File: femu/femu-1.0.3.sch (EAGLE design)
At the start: 54 parts, among them IC1 ESP32-QFN_5X5

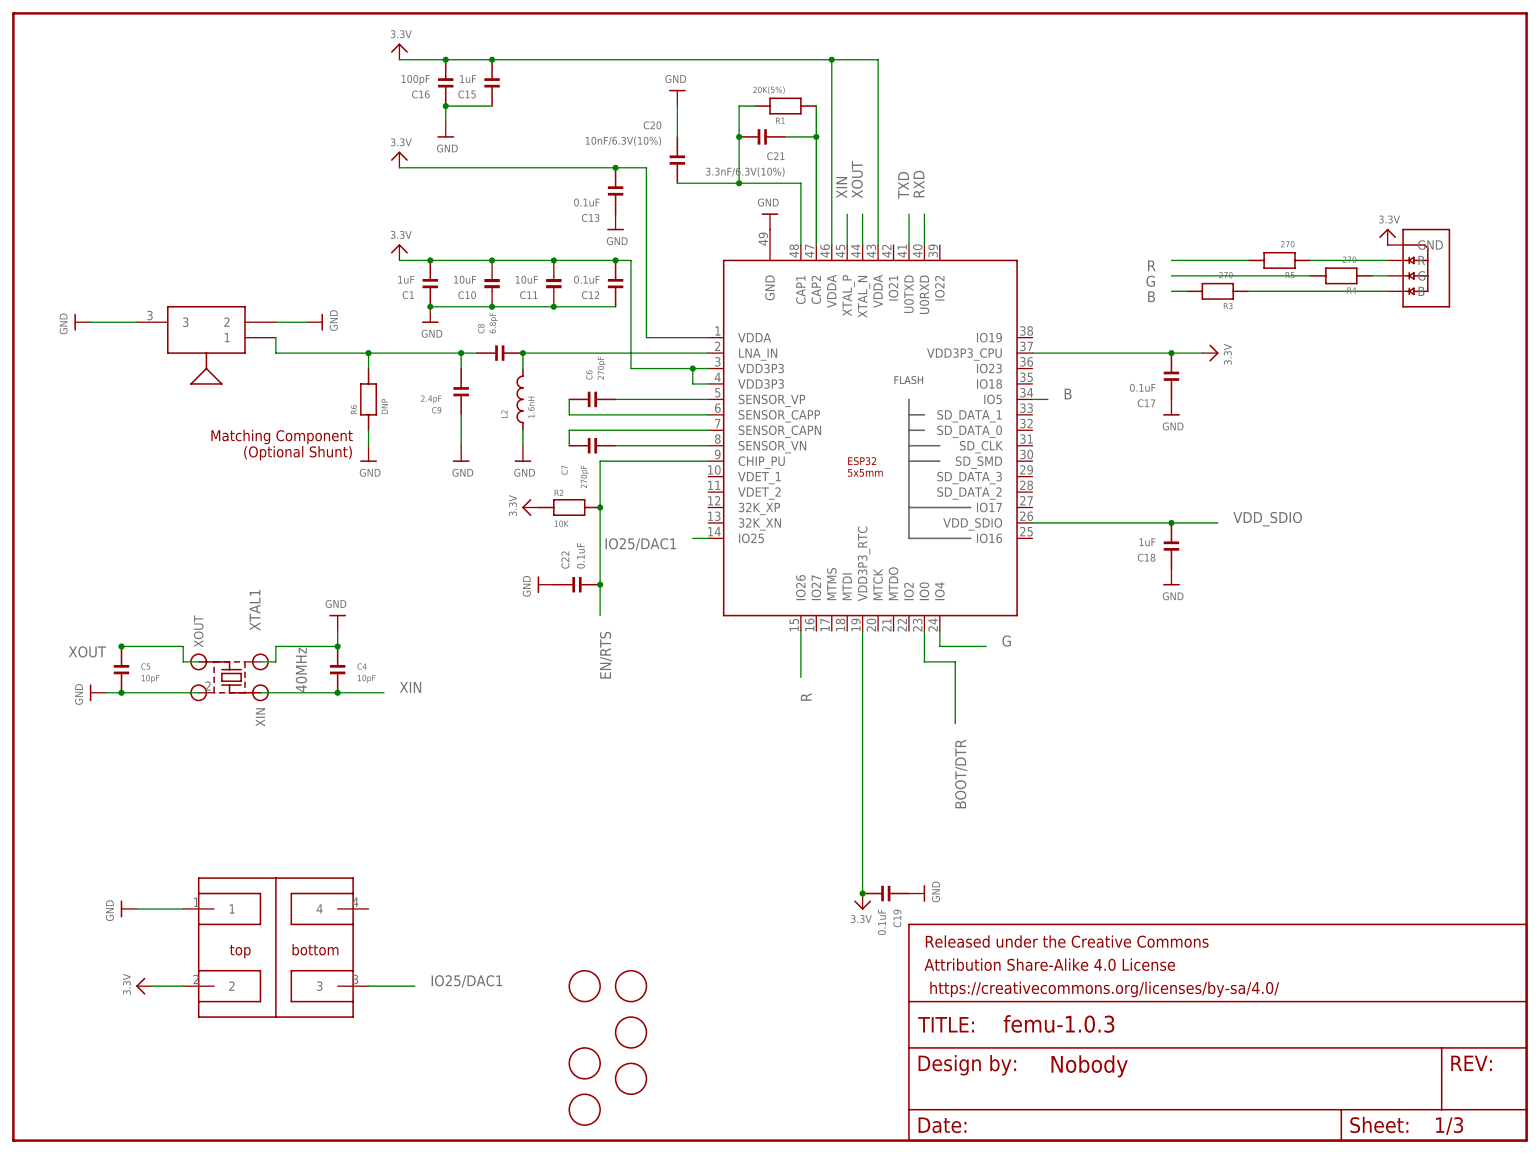
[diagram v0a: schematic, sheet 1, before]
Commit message: Adding work on femu 1.0.2, and 1.0.3
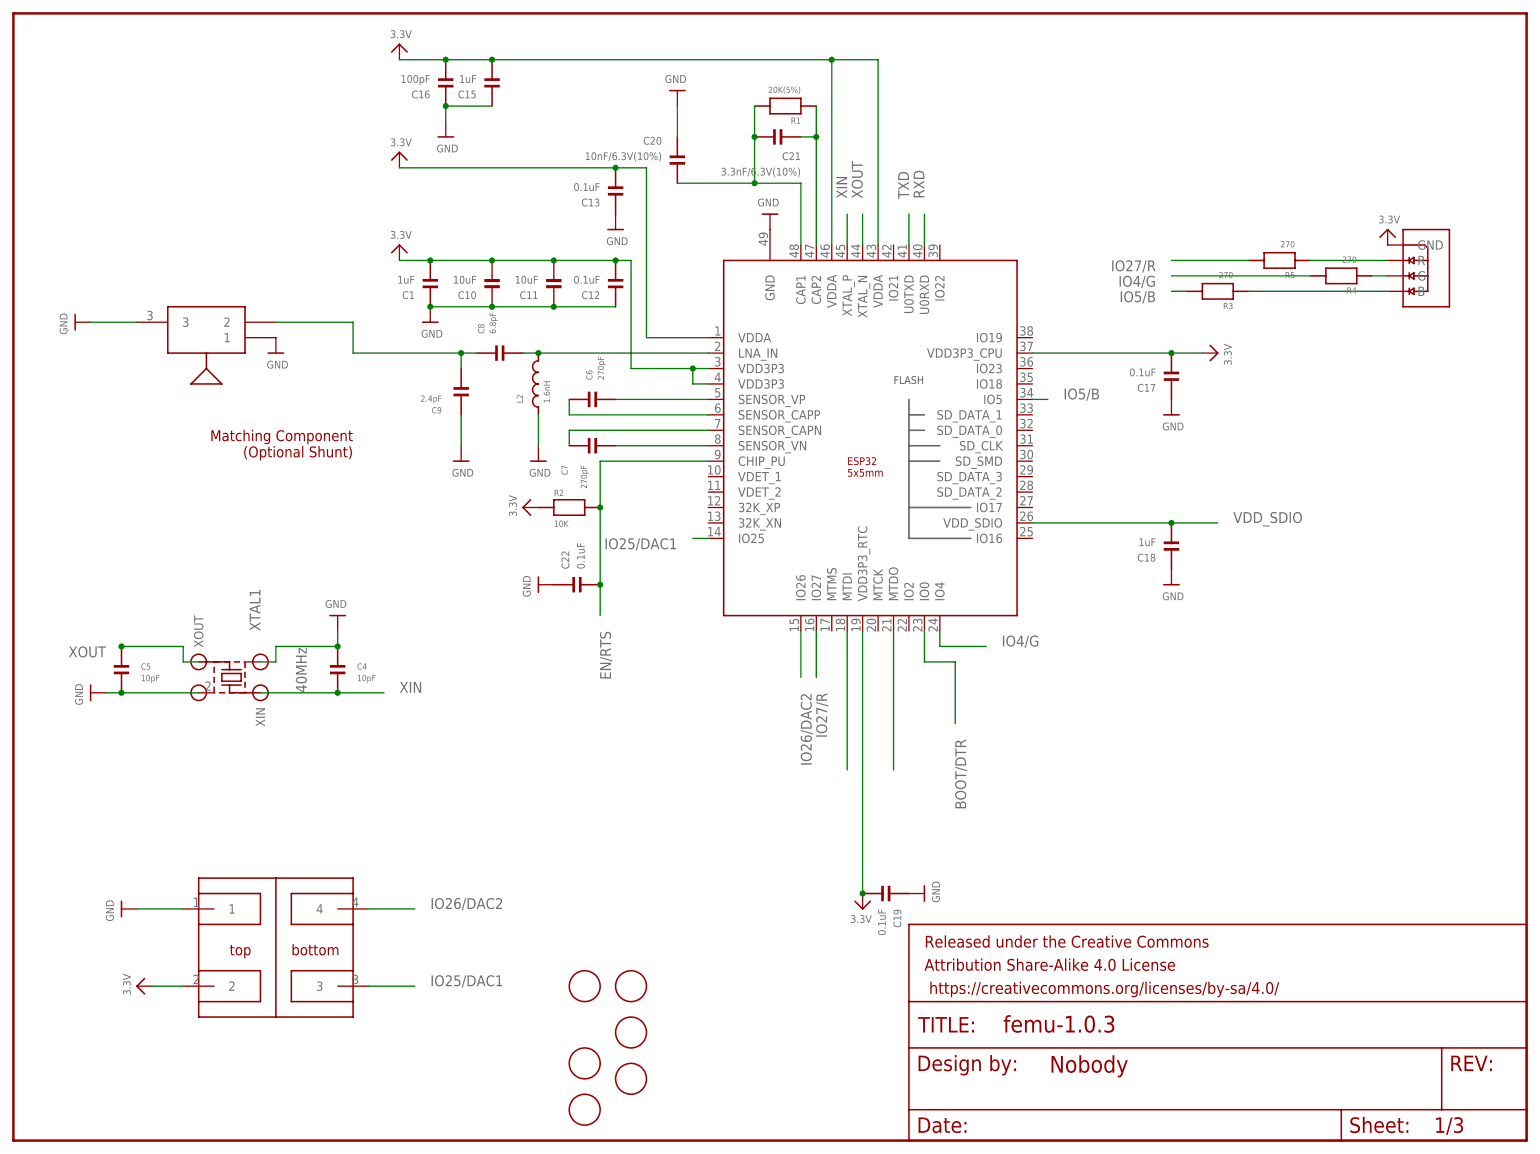
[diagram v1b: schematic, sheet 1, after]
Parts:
- removed R6: DNP, parts_0201:RESISTOR_0201
- added FB2: (no value), microbuilder:FERRITE_0402MP
- added R16: 1K, parts_0201:RESISTOR_0201
- added R17: 560, parts_0201:RESISTOR_0201
- C1, C15, C18: MPN CL03A105KQ3CSNH -> 0201ZD105MAT2A
- C10, C11: MPN GRM155R60G106ME44D -> CL05A106MP5NUNC
- C12, C19, C22: MPN GRM033C80J104KE84D -> GRM033R61C104KE84D
- C13, C17: device parts_01005:CAPACITOR -> parts_0201:CAPACITOR_0201; MPN GRM022R60G104ME15L -> GRM033R61C104KE84D
- C2, C3: device parts_0201:CAPACITOR_0201 -> microbuilder:CAP_CERAMIC_0402MP
- C20: device parts_01005:CAPACITOR -> parts_0201:CAPACITOR_0201; MPN GRM022R60J103KE19L -> GRM033R60J103KA01D
- C23: device parts_0201:CAPACITOR_0201 -> microbuilder:CAP_CERAMIC_0402MP; MPN GRM035R60G475ME15D -> GRM035R60J475ME15D; SPICEPREFIX (none) -> C
- C24, C25, C28, C29: SPICEPREFIX (none) -> C
- C27: MPN GRM033C80J104KE84D -> GRM033R61C104KE84D; SPICEPREFIX (none) -> C
- C4, C5: MPN CC0201JRNPO9BN100 -> CBR02C120F3GAC
- FB1: SPICEPREFIX (none) -> F
- R1: device parts_01005:RESISTOR -> parts_0201:RESISTOR_0201; MPN RC0100JR-0720KL -> ERJ-1GNJ203C
- R8, R9: SPICEPREFIX (none) -> R
- U$11, U$37: SPICEPREFIX (none) -> U
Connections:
- net B renamed IO5/B
- net G renamed IO4/G
- removed net R: IC1.IO26, R5.2
- new net IO26/DAC2: IC1.IO26, U$6.4
- new net IO27/R: IC1.IO27, R5.2
- new net N$11: FB2.P$1, U$37.GND
- new net N$12: IC1.MTDI
- new net N$13: IC1.MTDO
- new net N$14: LDO1.B1/EN, R16.2, R17.2
- net GND: now also ANT1.1, FB2.P$2, R17.1; no longer ANT1.2, R6.1, U$37.GND
- net N$6: now also ANT1.2; no longer ANT1.1, R6.2
- net VIN: now also R16.1; no longer LDO1.B1/EN
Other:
- moved on the sheet: C21, L2

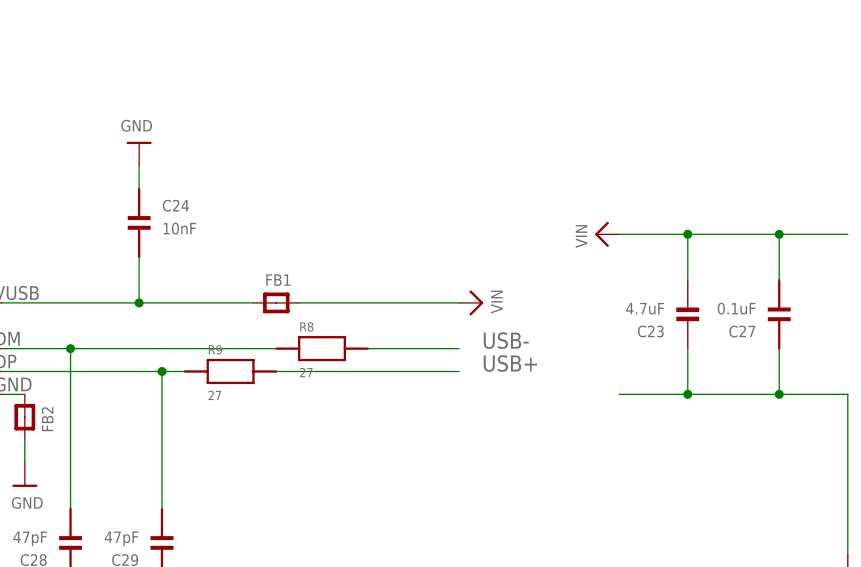
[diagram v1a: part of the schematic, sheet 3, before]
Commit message: Adjusting MPNs for FEMU 1.0.3
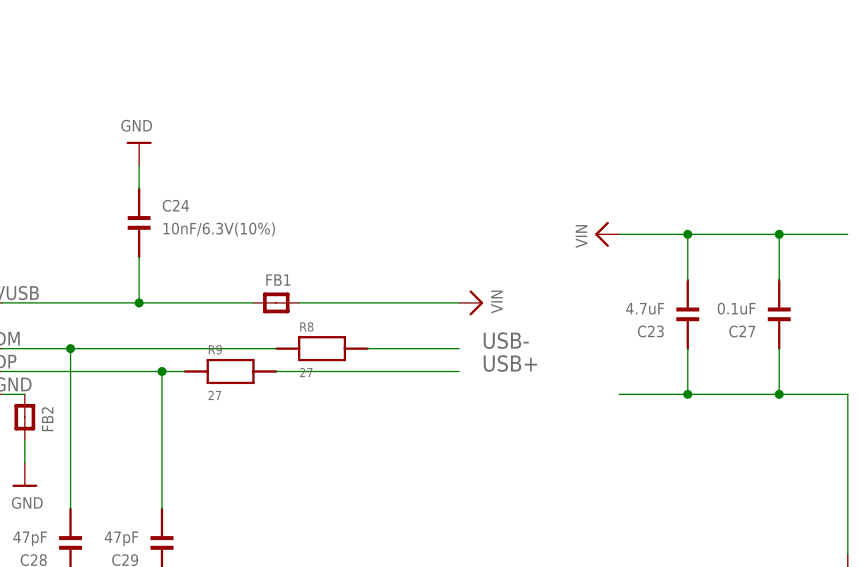
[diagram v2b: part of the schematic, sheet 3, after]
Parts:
- C1, C15, C18: MPN 0201ZD105MAT2A -> CL03A105KQ3CSNH
- C2, C3: MPN 0201ZD105MAT2A -> CL05A105KO5NNNC
- C23: device microbuilder:CAP_CERAMIC_0402MP -> parts_0201:CAPACITOR_0201
- C24: value 10nF -> 10nF/6.3V(10%); MPN GRM033R71A103KA01D -> GRM033R60J103KA01D; SPICEPREFIX C -> (none)
- C25: MPN GRM033C80J104KE84D -> GRM033R61C104KE84D; SPICEPREFIX C -> (none)
- C27: SPICEPREFIX C -> (none)
- C4, C5: MPN CBR02C120F3GAC -> CC0201JRNPO9BN100
- LDO1: MPN NCP167AFCT330T2G -> NCP167BFCT330T2G
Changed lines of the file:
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@@
 </part>
 <part name="C1" library="parts_0201" deviceset="CAPACITOR_0201" device="" value="1uF">
-<attribute name="MPN" value="0201ZD105MAT2A"/>
+<attribute name="MPN" value="CL03A105KQ3CSNH"/>
 </part>
 <part name="XTAL1" library="crystals" deviceset="ABM12" device="" value="40MHz">
@@
 </part>
 <part name="C4" library="parts_0201" deviceset="CAPACITOR_0201" device="" value="10pF">
-<attribute name="MPN" value="CBR02C120F3GAC"/>
+<attribute name="MPN" value="CC0201JRNPO9BN100"/>
 </part>
 <part name="C5" library="parts_0201" deviceset="CAPACITOR_0201" device="" value="10pF">
-<attribute name="MPN" value="CBR02C120F3GAC"/>
+<attribute name="MPN" value="CC0201JRNPO9BN100"/>
 </part>
 <part name="U$7" library="microbuilder" deviceset="GND" device=""/>
@@
 <part name="U$16" library="microbuilder" deviceset="GND" device=""/>
 <part name="C15" library="parts_0201" deviceset="CAPACITOR_0201" device="" value="1uF">
-<attribute name="MPN" value="0201ZD105MAT2A"/>
+<attribute name="MPN" value="CL03A105KQ3CSNH"/>
 </part>
 <part name="C16" library="parts_0201" deviceset="CAPACITOR_0201" device="" value="100pF">
@@
 <part name="U$21" library="microbuilder" deviceset="GND" device=""/>
 <part name="C18" library="parts_0201" deviceset="CAPACITOR_0201" device="" value="1uF">
-<attribute name="MPN" value="0201ZD105MAT2A"/>
+<attribute name="MPN" value="CL03A105KQ3CSNH"/>
 </part>
 <part name="U$26" library="microbuilder" deviceset="GND" device=""/>
@@
 </part>
 <part name="C25" library="parts_0201" deviceset="CAPACITOR_0201" device="" value="0.1uF">
-<attribute name="MPN" value="GRM033C80J104KE84D"/>
-<attribute name="SPICEPREFIX" value="C"/>
+<attribute name="MPN" value="GRM033R61C104KE84D"/>
 </part>
 <part name="C27" library="parts_0201" deviceset="CAPACITOR_0201" device="" value="0.1uF">
 <attribute name="MPN" value="GRM033R61C104KE84D"/>
-<attribute name="SPICEPREFIX" value="C"/>
 </part>
 <part name="U$37" library="usb-type-a-pcb-footprint-only" deviceset="USB-A-PCB" device="">
@@
 <attribute name="SPICEPREFIX" value="F"/>
 </part>
-<part name="C23" library="microbuilder" deviceset="CAP_CERAMIC" device="_0402MP" value="4.7uF">
+<part name="C23" library="parts_0201" deviceset="CAPACITOR_0201" device="" value="4.7uF">
 <attribute name="MPN" value="GRM035R60J475ME15D"/>
 <attribute name="SPICEPREFIX" value="C"/>
 </part>
-<part name="C24" library="parts_0201" deviceset="CAPACITOR_0201" device="" value="10nF">
-<attribute name="MPN" value="GRM033R71A103KA01D"/>
-<attribute name="SPICEPREFIX" value="C"/>
+<part name="C24" library="parts_0201" deviceset="CAPACITOR_0201" device="" value="10nF/6.3V(10%)">
+<attribute name="MPN" value="GRM033R60J103KA01D"/>
 </part>
 <part name="U$20" library="microbuilder" deviceset="VIN" device=""/>
@@
 <part name="FID6" library="adafruit" deviceset="FIDUCIAL" device=""/>
 <part name="LDO1" library="onsemi" deviceset="NCP167AFCT330T2G" device="">
-<attribute name="MPN" value="NCP167AFCT330T2G"/>
+<attribute name="MPN" value="NCP167BFCT330T2G"/>
 </part>
 <part name="C2" library="microbuilder" deviceset="CAP_CERAMIC" device="_0402MP" value="1uF">
-<attribute name="MPN" value="0201ZD105MAT2A"/>
+<attribute name="MPN" value="CL05A105KO5NNNC"/>
 </part>
 <part name="C3" library="microbuilder" deviceset="CAP_CERAMIC" device="_0402MP" value="1uF">
-<attribute name="MPN" value="0201ZD105MAT2A"/>
+<attribute name="MPN" value="CL05A105KO5NNNC"/>
 </part>
 <part name="U$34" library="microbuilder" deviceset="3.3V" device=""/>
